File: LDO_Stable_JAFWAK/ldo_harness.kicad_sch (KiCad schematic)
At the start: 26 parts, among them J12 EN_FG, J16 VDD_SEL, J18 EN_SEL, J5 EN_AIN_SEL, U1 SU272AFJK_LDO, U6 FXLP34, U8 FXLP34

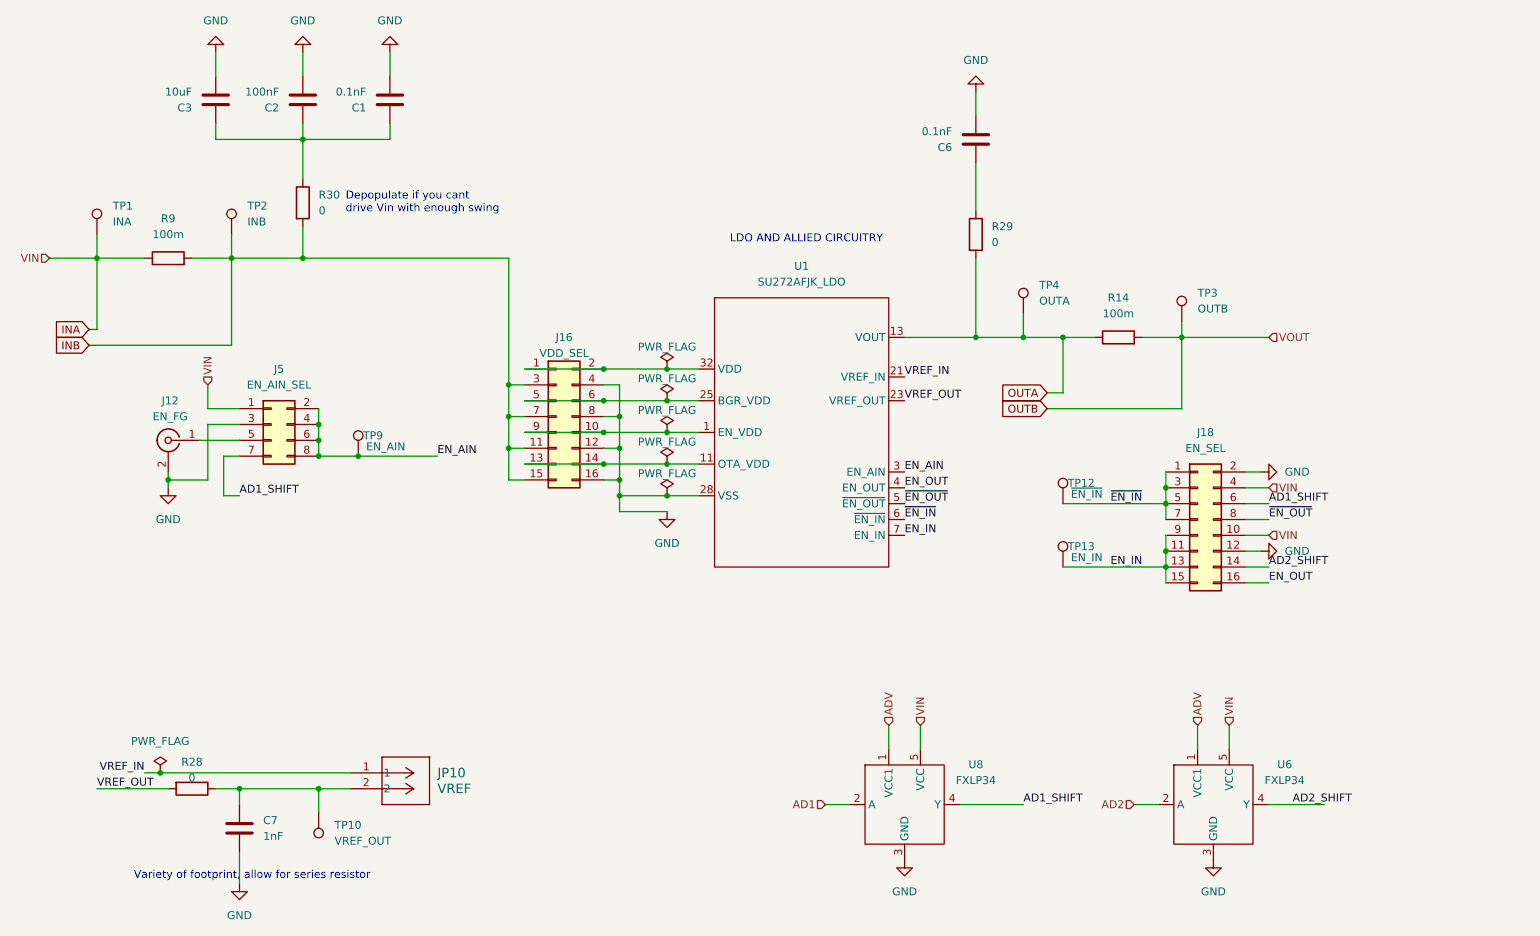
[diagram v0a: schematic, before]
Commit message: Several Changes
Moved temp sensor closer to chip
Add silkscreen
Moved capacitors closer to chip
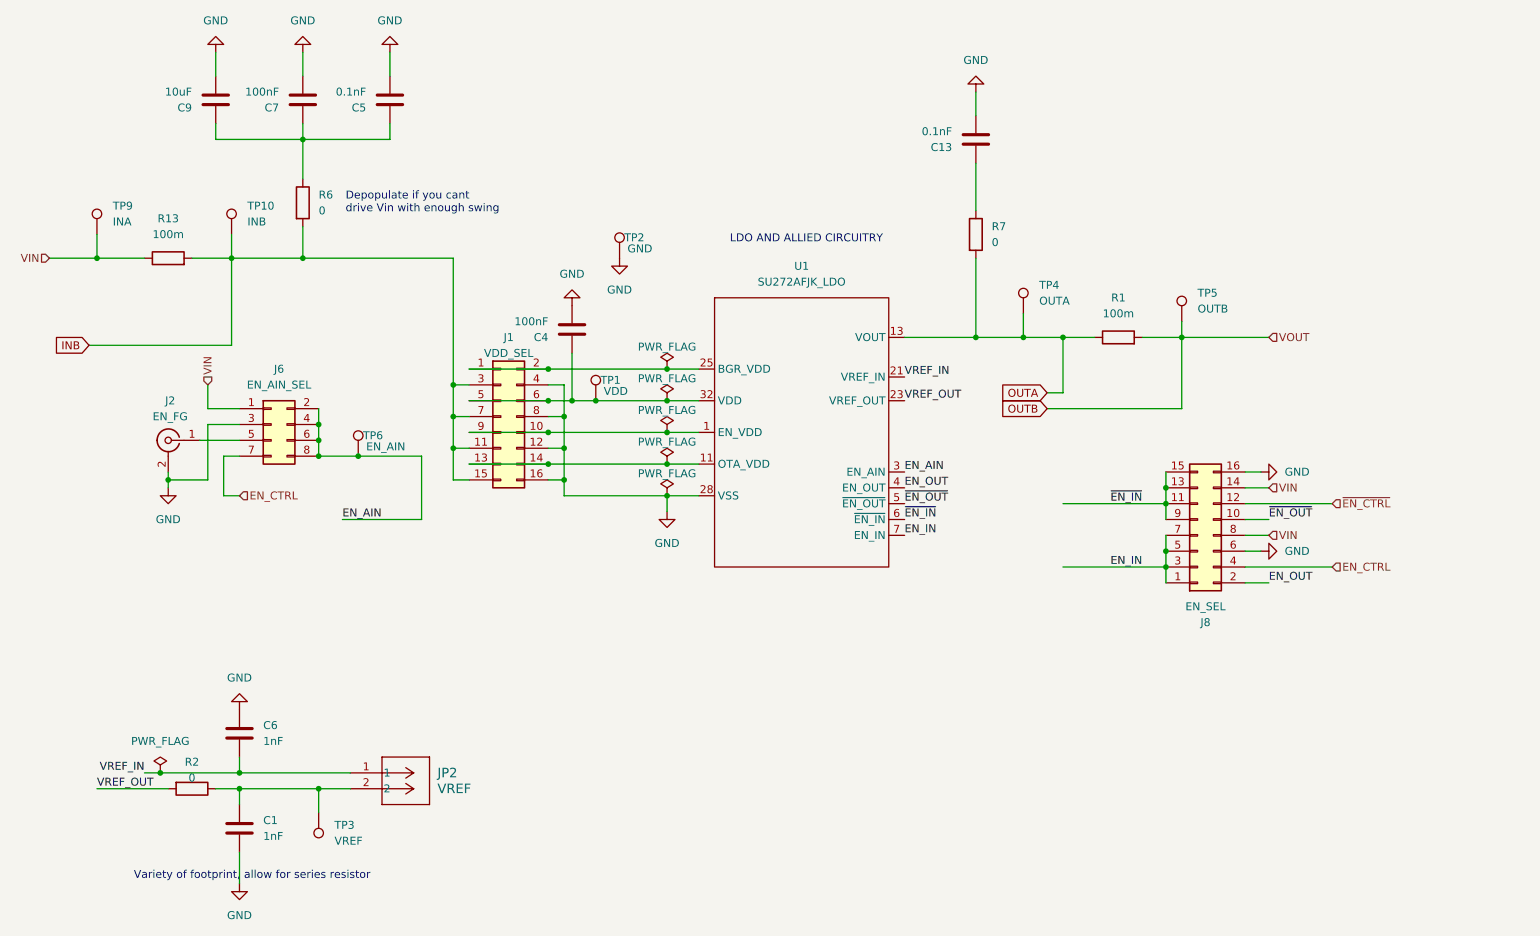
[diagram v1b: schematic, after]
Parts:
- removed TP12: ~{EN_IN}, TPS7A7001_Evaluation_Board_footprint_lib:KEYSTONE_5016, symbol Connector:TestPoint
- removed TP13: EN_IN, TPS7A7001_Evaluation_Board_footprint_lib:KEYSTONE_5016, symbol Connector:TestPoint
- removed U6, U8: FXLP34, Package_TO_SOT_SMD:SOT-353_SC-70-5, symbol JAFWAK:FXLP34
- added C4: 100nF, Capacitor_SMD:C_0805_2012Metric_Pad1.18x1.45mm_HandSolder, symbol Device:C
- added C6: 1nF, Capacitor_SMD:C_0805_2012Metric_Pad1.18x1.45mm_HandSolder, symbol Device:C
- added TP1: VDD, TPS7A7001_Evaluation_Board_footprint_lib:KEYSTONE_5016, symbol Connector:TestPoint
- added TP2: GND, TPS7A7001_Evaluation_Board_footprint_lib:KEYSTONE_5016, symbol Connector:TestPoint
- C1: renamed from C7; KiLib_Generator (none) -> SMD_2terminal_chip_molded
- C13: renamed from C6; KiLib_Generator (none) -> SMD_2terminal_chip_molded
- C5: renamed from C1; KiLib_Generator (none) -> SMD_2terminal_chip_molded
- C7: renamed from C2; KiLib_Generator (none) -> SMD_2terminal_chip_molded
- C9: renamed from C3; KiLib_Generator (none) -> SMD_2terminal_chip_molded
- J1: renamed from J16; KiLib_Generator (none) -> connector/pin_header_socket
- J6: renamed from J5; KiLib_Generator (none) -> connector/pin_header_socket
- J8: renamed from J18; KiLib_Generator (none) -> connector/pin_header_socket
- JP2: renamed from JP10; KiLib_Generator (none) -> connector/pin_header_socket
- R1: renamed from R14; KiLib_Generator (none) -> SMD_2terminal_chip_molded
- R13: renamed from R9; KiLib_Generator (none) -> SMD_2terminal_chip_molded
- R2: renamed from R28; KiLib_Generator (none) -> SMD_2terminal_chip_molded
- R6: renamed from R30; KiLib_Generator (none) -> SMD_2terminal_chip_molded
- R7: renamed from R29; KiLib_Generator (none) -> SMD_2terminal_chip_molded
- TP3: renamed from TP10; value VREF_OUT -> VREF
- U1: KiLib_Generator (none) -> package/no_lead
- renumbered J12 to J2, TP2 to TP10, TP3 to TP5, TP9 to TP6, TP1 to TP9
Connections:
- net BGR_VDD: now also J1.1 (Pin_1), J1.2 (Pin_2); no longer J1.5 (Pin_5), J1.6 (Pin_6)
- net EN_IN: now also J8.1 (Pin_1), J8.3 (Pin_3), J8.5 (Pin_5), J8.7 (Pin_7); no longer J8.11 (Pin_11), J8.13 (Pin_13), J8.15 (Pin_15), J8.9 (Pin_9)
- net EN_OUT: now also J8.2 (Pin_2); no longer J8.16 (Pin_16)
- net GND: now also J8.16 (Pin_16), J8.6 (Pin_6), C4.2, C6.1, TP2.1; no longer J8.12 (Pin_12), J8.2 (Pin_2)
- net VDD: now also J1.5 (Pin_5), J1.6 (Pin_6), C4.1, TP1.1; no longer J1.1 (Pin_1), J1.2 (Pin_2)
- net VREF_IN: now also C6.2
- net ~{EN_IN}: now also J8.11 (Pin_11), J8.13 (Pin_13), J8.15 (Pin_15), J8.9 (Pin_9); no longer J8.1 (Pin_1), J8.3 (Pin_3), J8.5 (Pin_5), J8.7 (Pin_7)
- net ~{EN_OUT}: now also J8.10 (Pin_10); no longer J8.8 (Pin_8)
- net AD1_SHIFT renamed EN_CTRL
- net EN_CTRL: now also J8.4 (Pin_4); no longer J8.6 (Pin_6)
- net AD2_SHIFT renamed VIN
- net VIN: now also J6.1 (Pin_1), J8.8 (Pin_8), R13.1, TP9.1
- removed net INA: J6.1 (Pin_1), J8.10 (Pin_10), J8.4 (Pin_4), R13.1, TP9.1
- new net ~{EN_CTRL}: J8.12 (Pin_12)
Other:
- moved on the sheet: J1

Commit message: Couple changes
More caps
Series Resitors
Stiching Vias
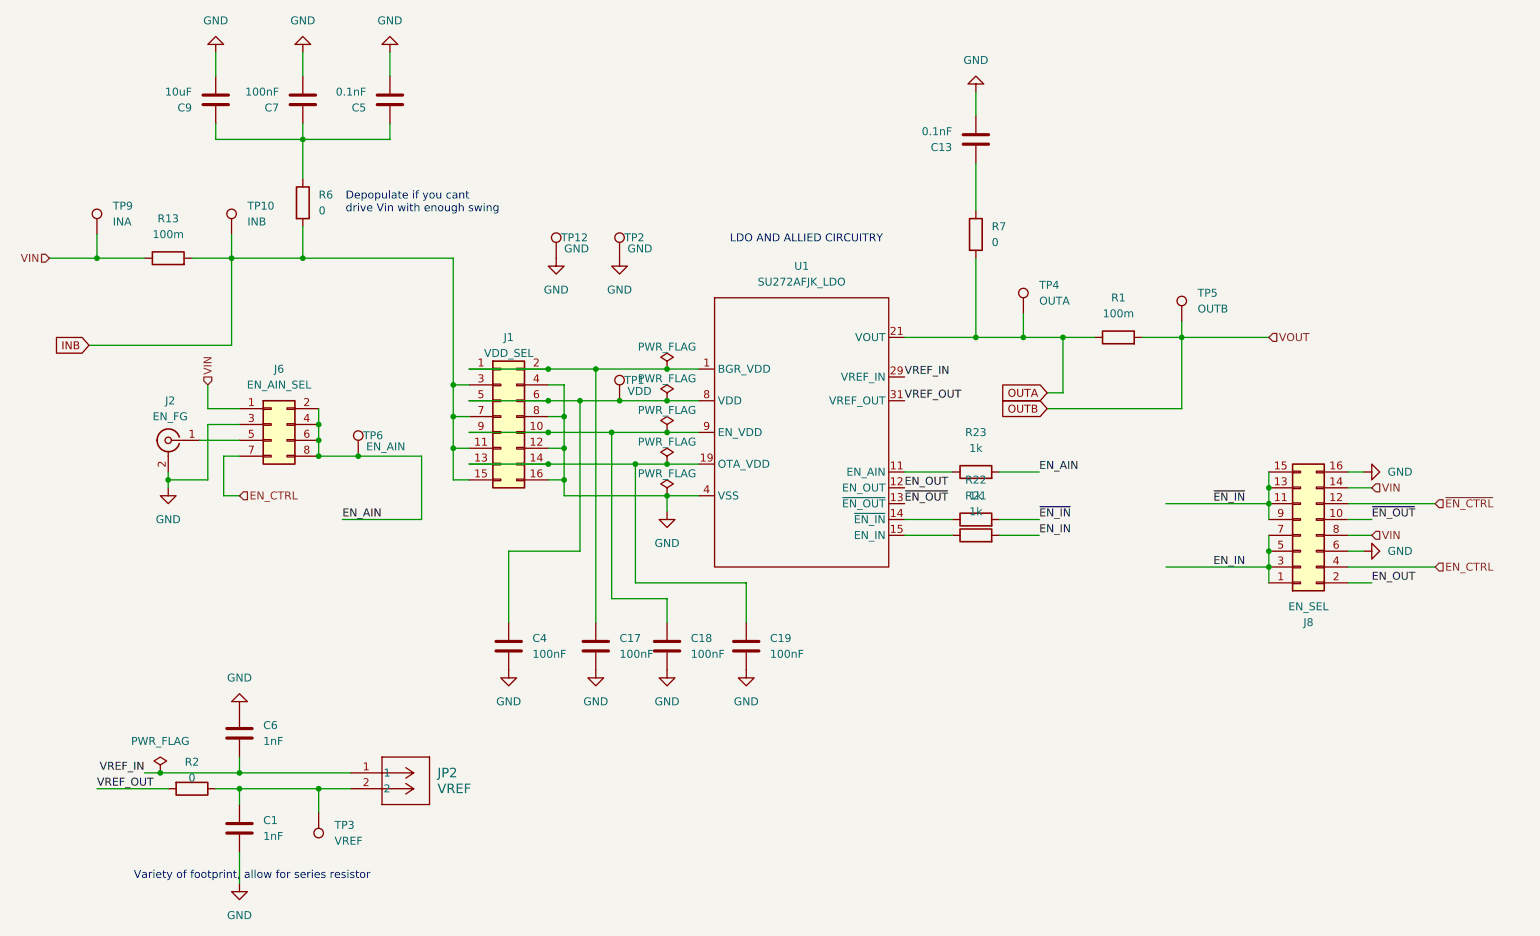
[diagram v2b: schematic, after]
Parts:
- added C17, C18, C19: 100nF, Capacitor_SMD:C_0603_1608Metric, symbol Device:C
- added R21, R22, R23: 1k, Resistor_SMD:R_0603_1608Metric, symbol Device:R
- added TP12: GND, TPS7A7001_Evaluation_Board_footprint_lib:KEYSTONE_5016, symbol Connector:TestPoint
- C4: footprint Capacitor_SMD:C_0805_2012Metric_Pad1.18x1.45mm_HandSolder -> Capacitor_SMD:C_0603_1608Metric
- U1: footprint Package_DFN_QFN:QFN-32-1EP_7x7mm_P0.65mm_EP5.4x5.4mm -> Package_DFN_QFN:QFN-32-1EP_7x7mm_P0.65mm_EP5.4x5.4mm_ThermalVias
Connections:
- net BGR_VDD: now also U1.1 (BGR_VDD), U1.2 (BGR_VDD), C17.1; no longer U1.25 (BGR_VDD), U1.26 (BGR_VDD)
- net EN_AIN: now also R23.2; no longer U1.3 (EN_AIN)
- net EN_IN: now also R21.2; no longer U1.7 (EN_IN)
- net EN_OUT: now also U1.12 (EN_OUT); no longer U1.4 (EN_OUT)
- net EN_VDD: now also U1.10 (EN_VDD), U1.9 (EN_VDD), C18.1; no longer U1.1 (EN_VDD), U1.2 (EN_VDD)
- net GND: now also U1.17 (VSS), U1.18 (VSS), U1.23 (VSS), U1.4 (VSS), U1.5 (VSS), U1.6 (VSS), U1.7 (VSS), C17.2, C18.2, C19.2, TP12.1; no longer U1.10 (VSS), U1.15 (VSS), U1.20 (VSS), U1.22 (VSS), U1.29 (VSS), U1.31 (VSS), U1.9 (VSS)
- net OTA_VDD: now also U1.19 (OTA_VDD), U1.20 (OTA_VDD), C19.1; no longer U1.11 (OTA_VDD), U1.12 (OTA_VDD)
- net OUTA: now also U1.21 (VOUT), U1.22 (VOUT); no longer U1.13 (VOUT), U1.14 (VOUT)
- net VDD: now also U1.25 (VDD), U1.26 (VDD), U1.3 (VDD); no longer U1.17 (VDD), U1.18 (VDD), U1.19 (VDD)
- net VREF_IN: now also U1.29 (VREF_IN); no longer U1.21 (VREF_IN)
- net VREF_OUT: now also U1.31 (VREF_OUT); no longer U1.23 (VREF_OUT)
- net ~{EN_IN}: now also R22.2; no longer U1.6 (~{EN_IN})
- net ~{EN_OUT}: now also U1.13 (~{EN_OUT}); no longer U1.5 (~{EN_OUT})
- new net: R22.1, U1.14 (~{EN_IN})
- new net: R21.1, U1.15 (EN_IN)
- new net: R23.1, U1.11 (EN_AIN)
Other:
- moved on the sheet: C4, J8, TP1
